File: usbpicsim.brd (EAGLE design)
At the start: 100 x 80 mm, 25 parts, among them U1 PIC16LF1455-I/ST

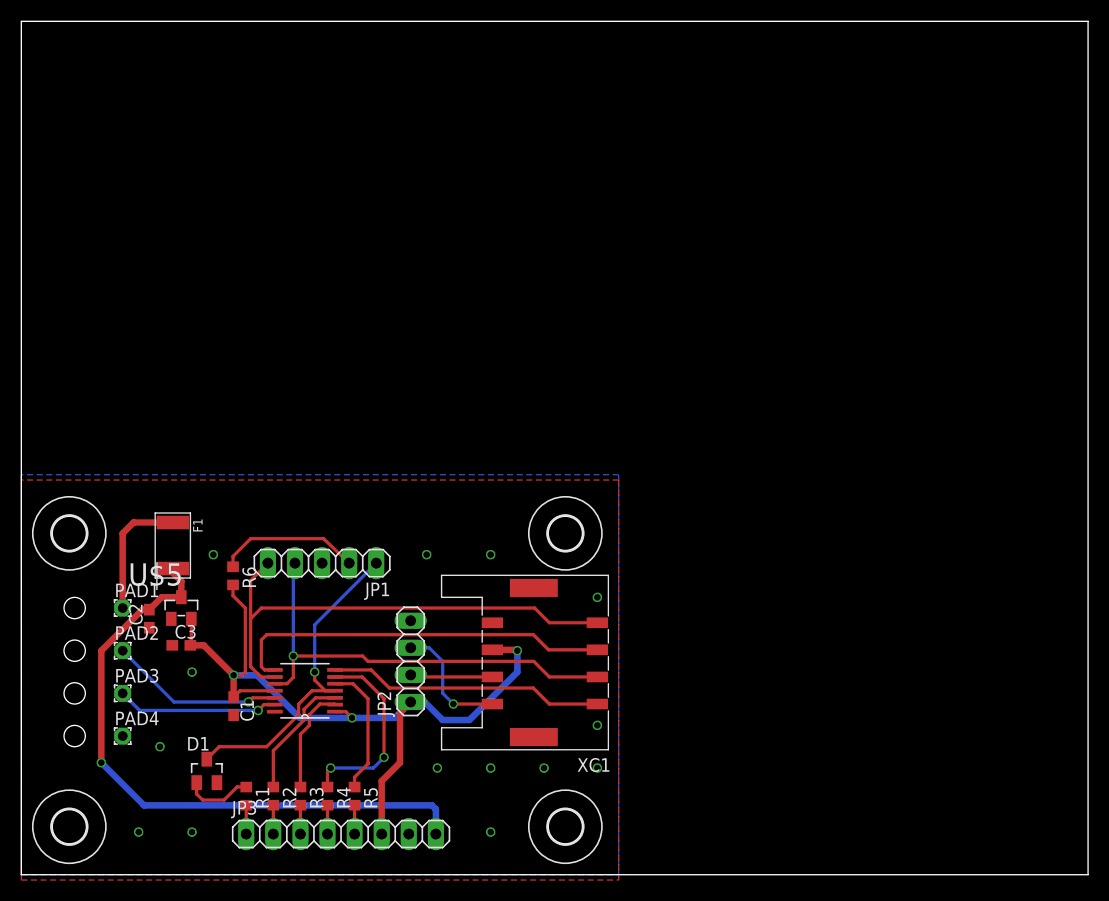
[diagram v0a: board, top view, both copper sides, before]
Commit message: More polishing of usbpicsim
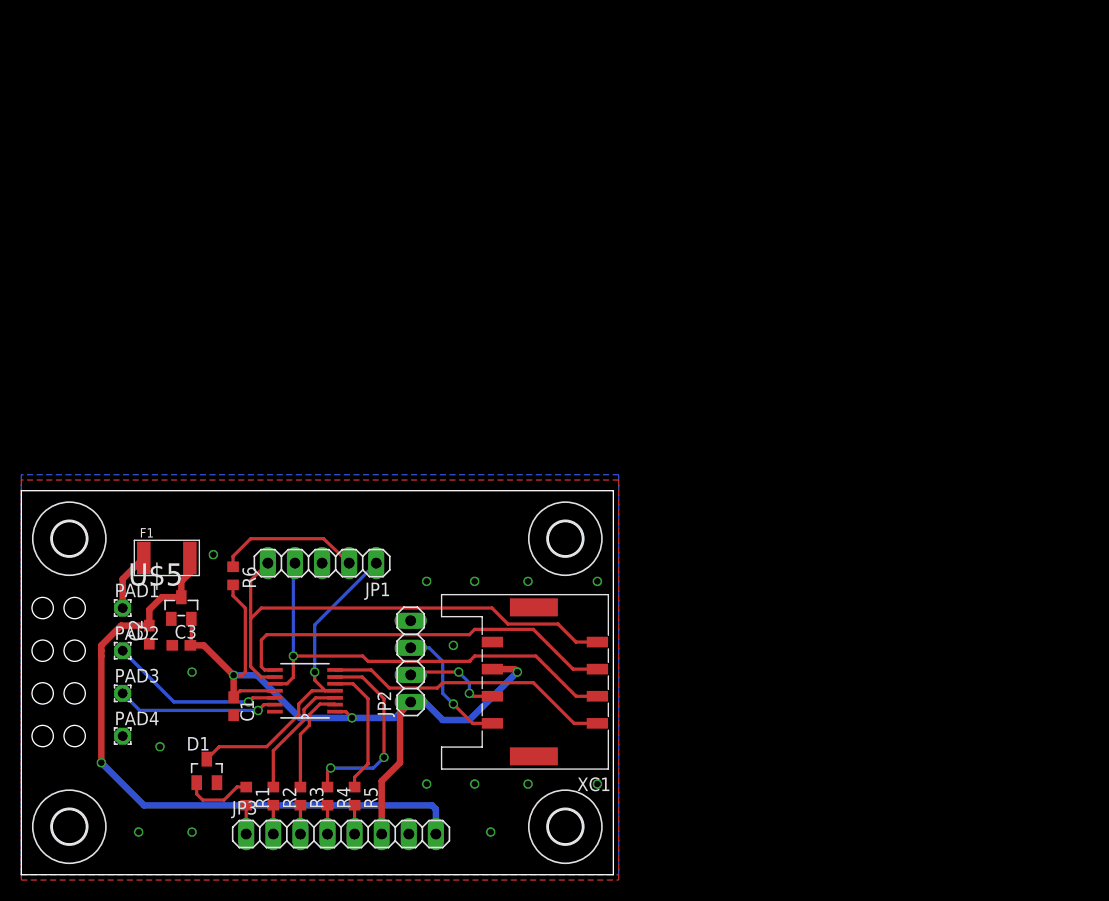
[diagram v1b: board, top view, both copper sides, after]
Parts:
- moved XC1 2.00 mm to (54.0, 18.0)
- moved C2 1.50 mm to (12.0, 22.5)
- moved F1 1.29 mm to (13.6, 29.7), turned to 0 degrees
- moved U$1 0.50 mm to (4.50, 31.5)
- moved U$3 0.50 mm to (51.0, 31.5)
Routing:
- net N$5: track 12.1 -> 5.52 mm
- net +5V: track 58.8 -> 60.8 mm
- net +3V3: track 74.9 -> 73.0 mm
- net +3V/IO: track 7.74 -> 9.30 mm, vias 0 -> 2
- net SPI_CLK: track 42.0 -> 43.2 mm
- net SPI_!SS: track 25.9 -> 27.1 mm
- net SPI_SDO: track 36.2 -> 37.4 mm
- net SPI_SDI: track 46.5 -> 47.3 mm
- net ADC/IO: track 11.6 -> 12.3 mm
- net GND: track 0.27 -> 0.00 mm, vias 14 -> 15
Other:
- board size 100 x 80 mm -> 55.5 x 36 mm

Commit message: Final usbpicsim board tuning
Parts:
- moved JP2 9.06 mm to (35.5, 29.0), turned to 180 degrees
- moved XC1 7.50 mm to (46.5, 18.0), flipped to the bottom, turned to 0 degrees
- moved C2 7.02 mm to (12.5, 15.5)
- moved C3 7.02 mm to (15.5, 14.5)
- moved U$5 7.02 mm to (15.5, 18.0)
- moved U$3 6.50 mm to (44.5, 31.5)
- moved U$4 6.50 mm to (44.5, 4.50)
- moved F1 4.87 mm to (14.2, 24.9), turned to 270 degrees
- moved JP1 4.20 mm to (24.0, 29.0)
- moved R6 4.03 mm to (17.8, 24.5)
- moved C1 0.50 mm to (19.4, 15.8)
- moved D1 0.50 mm to (16.9, 9.73)
- moved JP3 0.50 mm to (29.5, 3.81)
- moved PAD1 0.50 mm to (9.00, 25.0)
- moved PAD2 0.50 mm to (9.00, 21.0)
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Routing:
- net +5V: track 60.8 -> 50.1 mm, vias 1 -> 3
- net SPI_CLK: track 43.2 -> 36.0 mm, vias 1 -> 2
- net +3V3: track 73.0 -> 79.4 mm, vias 3 -> 5
- net SPI_!SS: track 27.1 -> 21.9 mm, vias 0 -> 1
- net ADC/IO: track 12.3 -> 8.15 mm, vias 1 -> 0
- net SPI_SDO: track 37.4 -> 33.5 mm, vias 0 -> 1
- net N$9: track 13.5 -> 17.3 mm
- net SPI_SDI: track 47.3 -> 49.4 mm, vias 0 -> 1
- net +3V/IO: track 9.30 -> 11.3 mm, vias 2 -> 1
- net RA3: track 30.0 -> 28.3 mm
- net N$5: track 5.52 -> 6.04 mm
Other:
- board size 55.5 x 36 mm -> 49 x 36 mm
- board text added: "-------"
- board text added: "USBPIC v1.0 r2016"
- board text added: "programator"

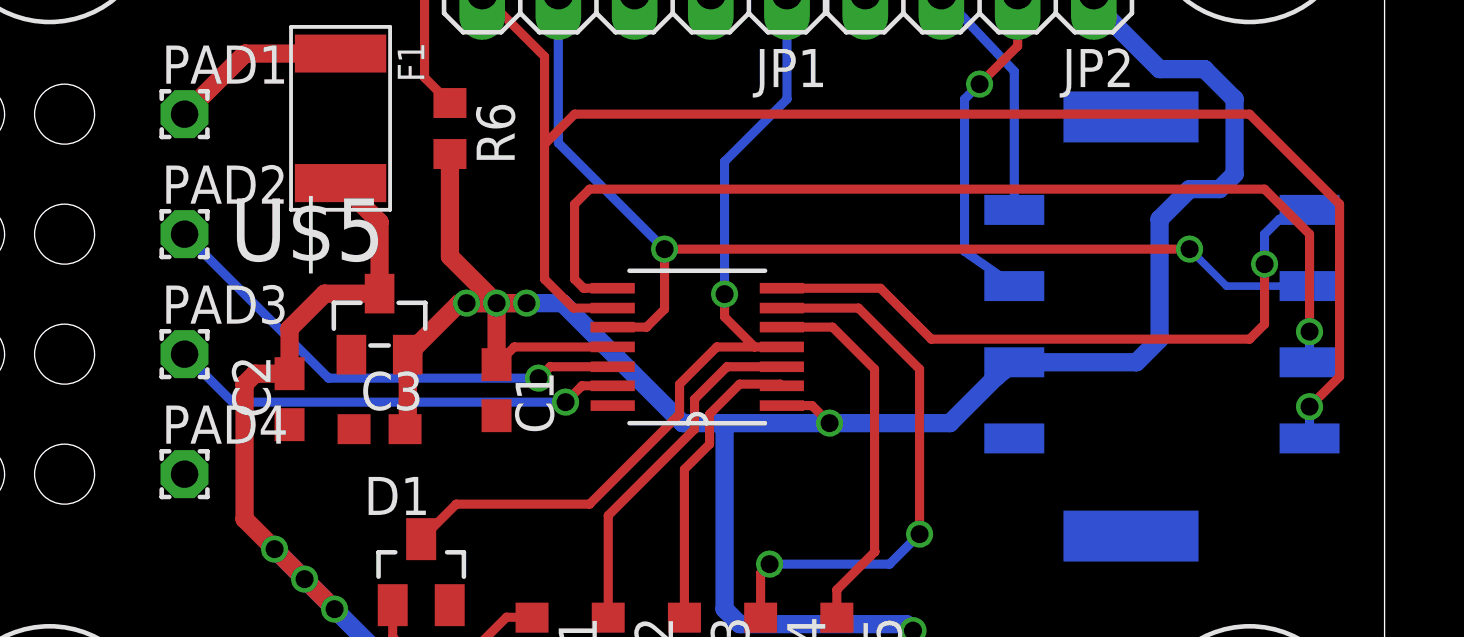
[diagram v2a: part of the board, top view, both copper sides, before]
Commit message: usbpicsim: improve vias clearance
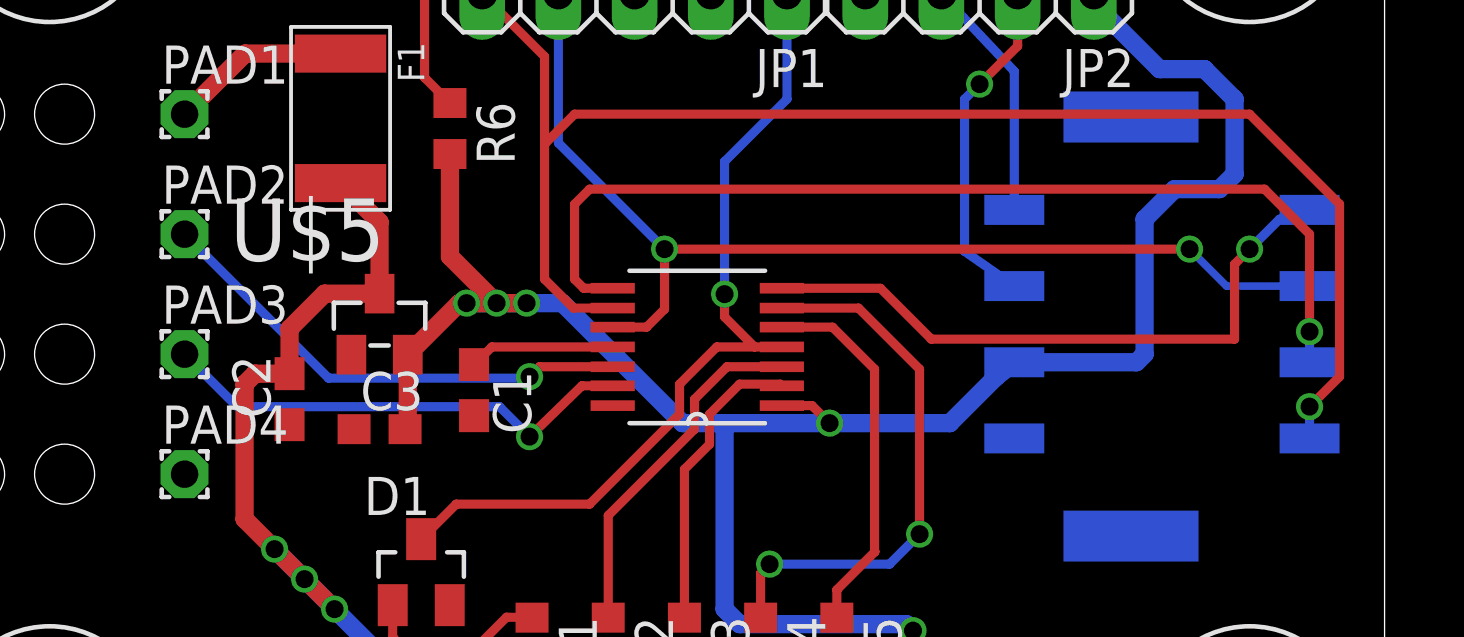
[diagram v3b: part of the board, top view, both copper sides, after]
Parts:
- moved C1 0.75 mm to (18.6, 15.8)
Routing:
- net +3V3: track 79.4 -> 78.4 mm
- net N$2: track 15.2 -> 16.1 mm
